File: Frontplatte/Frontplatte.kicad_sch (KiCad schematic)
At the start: 49 parts, among them J1 Conn_01x04_Male, J2 Conn_01x04_Male, J3 Conn_01x04_Male, J4 Conn_01x04_Male, J5 Conn_01x04_Male, SW1 SW_DIP_x04, U1 MCP23017_SP

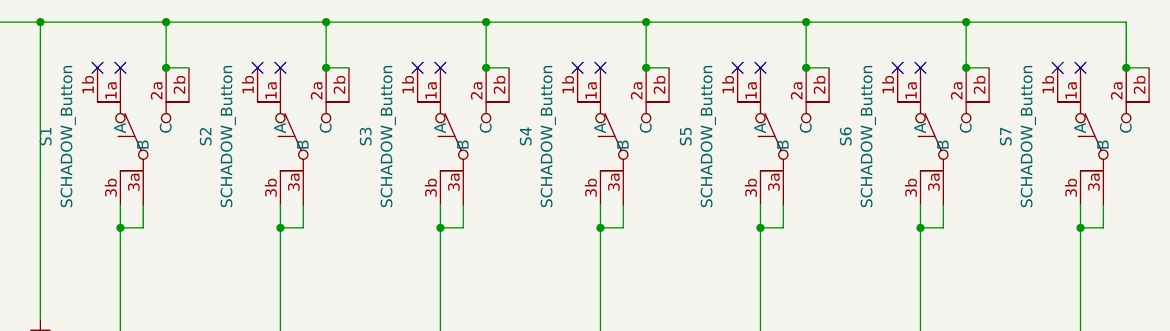
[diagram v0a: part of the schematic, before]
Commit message: Inserted 3D models into Front Plate
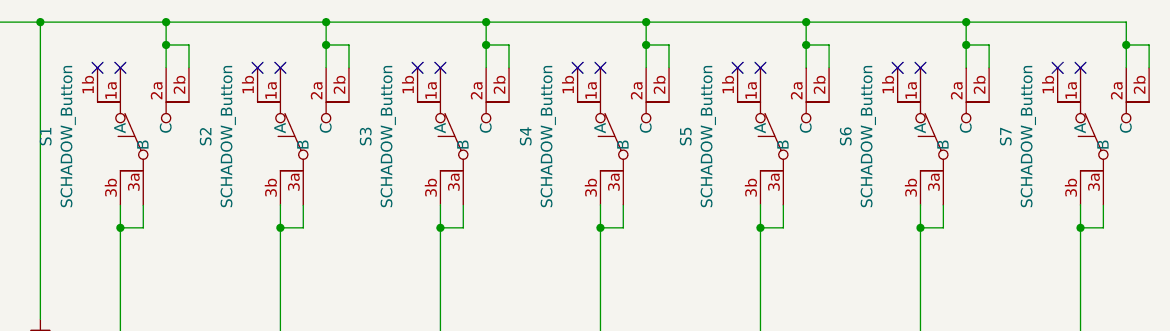
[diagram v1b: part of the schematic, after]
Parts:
- U1: footprint Package_DIP:DIP-28_W7.62mm -> Package_DIP:DIP-28_W7.62mm_LongPads
